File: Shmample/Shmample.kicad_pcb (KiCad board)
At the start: 2 copper layers, 127 x 127 mm, 148 parts, among them J1 Conn_01x04_Socket, J2 PowerOut, Q1 BC547, Q10 BC547, Q2 BC557, Q3 BC547, Q4 BC547, Q5 BC557, Q6 BC557, Q7 BC547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

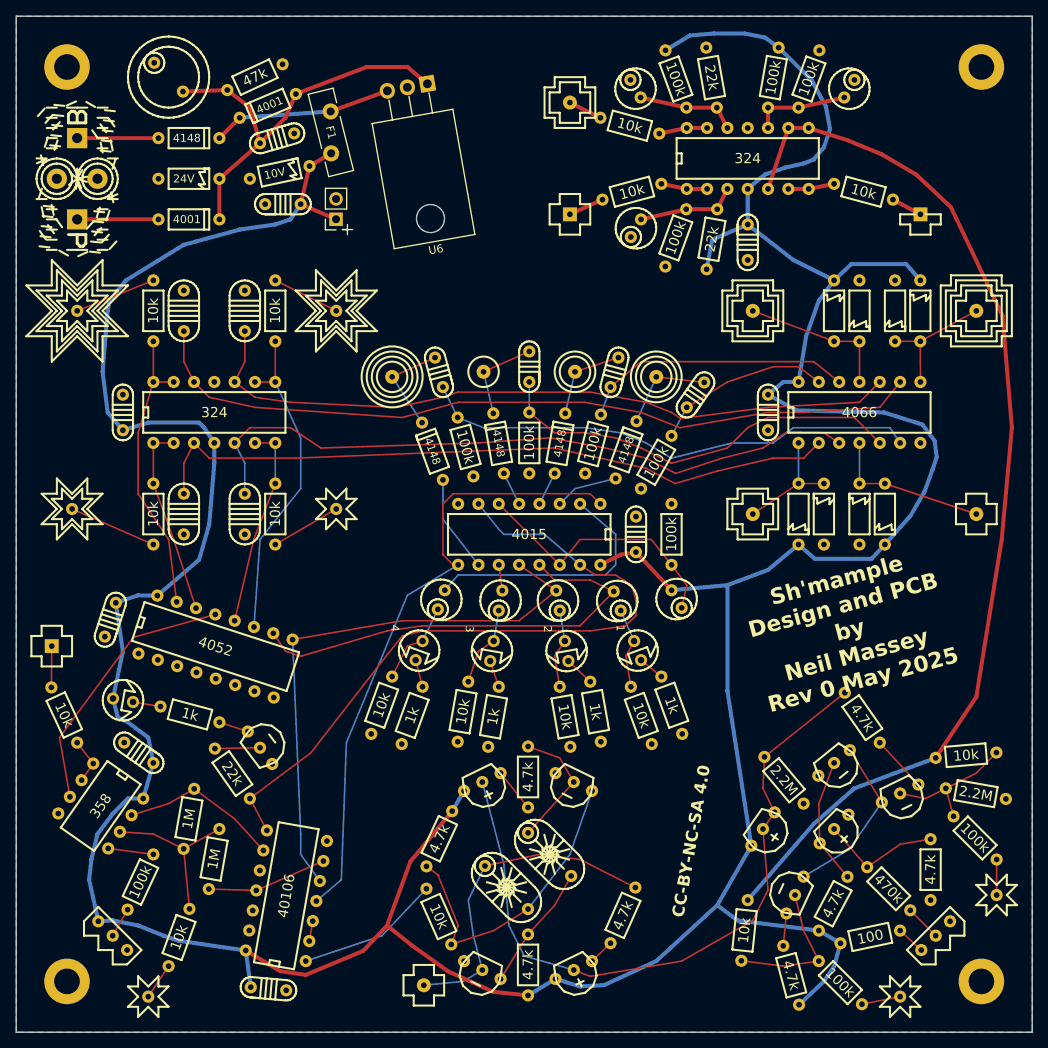
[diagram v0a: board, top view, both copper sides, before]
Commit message: Added attenuators
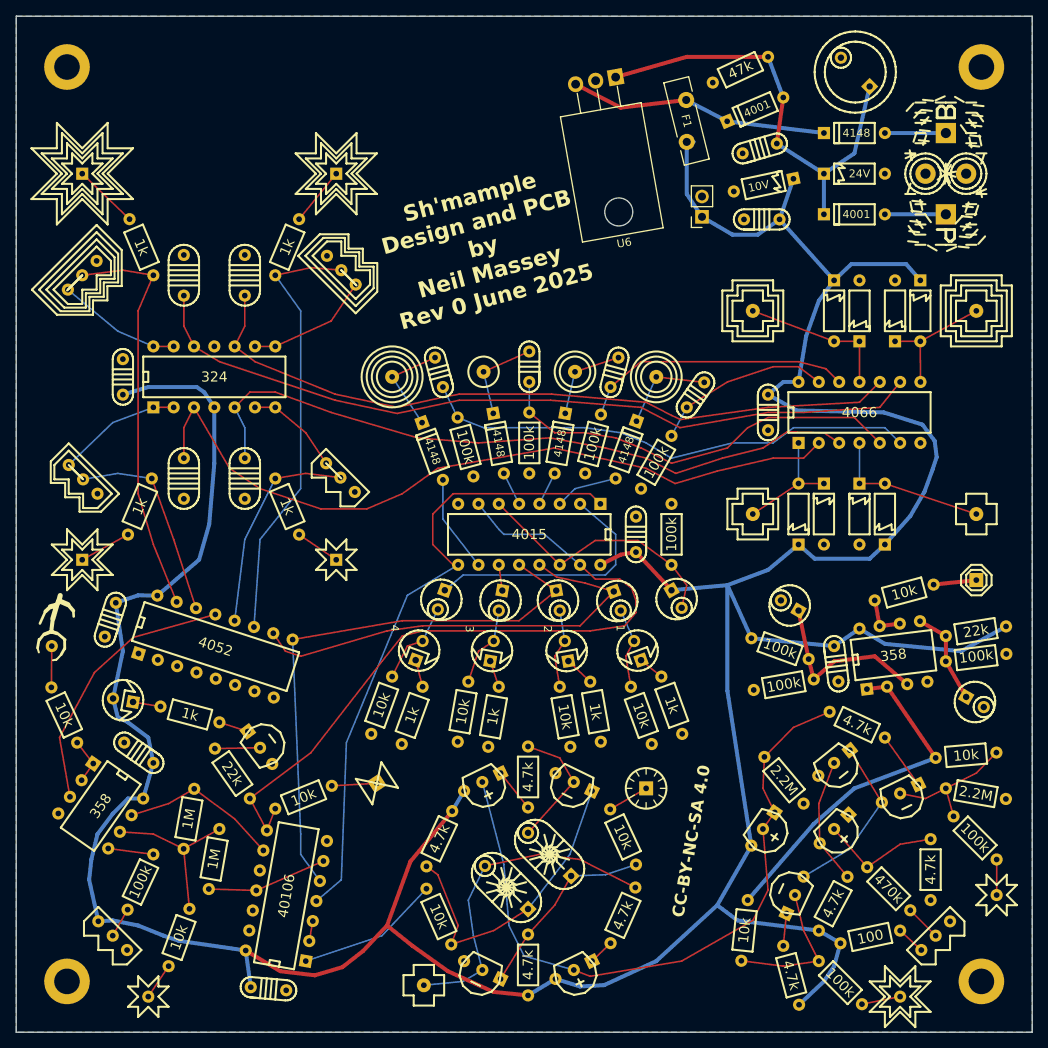
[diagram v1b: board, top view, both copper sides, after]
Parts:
- removed C18: 10uF, diy-nabra:cel1
- removed R40: 22k, diy-nabra:r3
- removed R51: 10k, diy-nabra:r3
- added RV3: 4_W, diy-nabra:wnob4, F.Cu at (19.2, 46.9)
- added RV4: 3_W, diy-nabra:wnob3, F.Cu at (55.1, 46.2)
- added RV5: 2_W, diy-nabra:wnob2, F.Cu at (19.3, 68.8)
- added RV6: 1_W, diy-nabra:wnob1, F.Cu at (51.4, 68.6)
- R33, R34, R35, R36: value 10k -> 1k
- R39: value 100k -> 10k
- TP1: footprint diy-nabra:wtrin -> diy-nabra:wtrin2
- TP12: value Lo -> Cmp-Out; footprint diy-nabra:wsqu2in -> diy-nabra:wcmp_out
- TP13: footprint diy-nabra:wsqout -> diy-nabra:wvout
- TP19: footprint diy-nabra:wsqout -> diy-nabra:wpod
- TP20: value MIDO -> Clk-Out; footprint diy-nabra:wsqout -> diy-nabra:wclk_out
- U1: value 324 -> 358; footprint diy-nabra:dip14 -> diy-nabra:dip8
- moved J1 108.6 mm to (128.9, 37.5)
- moved R49 97.1 mm to (45.1, 111.8), turned to 22 degrees
- moved R39 95.1 mm to (86.9, 111.8), turned to -65 degrees
- moved TP12 88.4 mm to (57.8, 108.6), turned to 33 degrees
- moved C19 85.8 mm to (115.8, 17.9)
- moved TP20 79.5 mm to (91.4, 109.2)
- moved D8 75.6 mm to (113.7, 32.4), turned to 0 degrees
- moved D6 75.6 mm to (113.7, 37.5), turned to 0 degrees
- moved D9 75.6 mm to (113.7, 27.3), turned to 0 degrees
- moved R3 73.9 mm to (104.6, 90.5), turned to -20 degrees
- moved C17 73.5 mm to (133.6, 99.1), turned to 150 degrees
- moved R4 71.5 mm to (112.4, 95.6), turned to -170 degrees
- moved TP13 68.3 mm to (132.7, 83.2)
- moved U1 66.2 mm to (118.1, 89.3), turned to 7 degrees
- moved C1 65.7 mm to (108.3, 85.7), turned to -30 degrees
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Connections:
- C1 pad 1: Net-(U1C-+) -> Net-(U1A-+)
- C17 pad 1: Net-(U1A-+) -> Net-(U1B-+)
- R3 pad 1: Net-(U1C-+) -> Net-(U1A-+)
- R33 pad 1: Net-(U5B--) -> Net-(U7-X0)
- R34 pad 1: Net-(U5A--) -> Net-(U7-X1)
- R35 pad 1: Net-(U5C--) -> Net-(U7-X3)
- R36 pad 1: Net-(U5D--) -> Net-(U7-X2)
- R37 pad 1: Net-(U1A-+) -> Net-(U1B-+)
- R38 pad 2: Net-(U1A-+) -> Net-(U1B-+)
- R39 pad 1: Net-(U1D-+) -> Net-(Q7-C)
- R39 pad 2: +9V -> Net-(R39-Pad2)
- R4 pad 2: Net-(U1C-+) -> Net-(U1A-+)
- R49 pad 2: Lo -> Data
- TP20 pad 1: Net-(R51-Pad1) -> Net-(R39-Pad2)
- U1 pad 1: Hi -> MIDO
- U1 pad 2: Hi -> MIDO
- U1 pad 4: +9V -> GND
- U1 pad 5: MIDO -> Net-(U1B-+)
- U1 pad 6: MIDO2 -> Hi
- U1 pad 7: MIDO2 -> Hi
- U1 pad 8: MIDO -> +9V
- U7 pad 11: Net-(U5C--) -> Net-(U7-X3)
- U7 pad 12: Net-(U5B--) -> Net-(U7-X0)
- U7 pad 14: Net-(U5A--) -> Net-(U7-X1)
- U7 pad 15: Net-(U5D--) -> Net-(U7-X2)
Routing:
- net MIDO: track 133.6 -> 43.5 mm
- net Net-(U7-X3): track 0.00 -> 55.2 mm
- net Net-(U7-X2): track 0.00 -> 51.0 mm
- net +9V: track 498.4 -> 456.8 mm
- net Net-(U7-X0): track 0.00 -> 27.0 mm
- net Net-(U7-X1): track 0.00 -> 25.8 mm
- net Net-(U5C--): track 40.7 -> 15.7 mm
- net Net-(U5D--): track 36.6 -> 15.5 mm
- net Net-(U5B--): track 25.5 -> 12.1 mm
- net Net-(U1D-+): track 12.5 -> 0.00 mm
- net Net-(U1C-+): track 12.2 -> 0.00 mm
- net Net-(U1B-+): track 0.00 -> 12.0 mm
- net Net-(U1A-+): track 12.5 -> 22.7 mm
- net Net-(D7-K): track 22.5 -> 32.5 mm
- net Net-(U5A--): track 24.1 -> 15.6 mm
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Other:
- board text added: "Sh'mample Design and PCB by Neil Massey Rev 0 June 2025"
- board text removed: "Sh'mample Design and PCB by Neil Massey Rev 0 May 2025"

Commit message: Revision
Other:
- board text added: "SAnnddmedaedSalAHHHHdSedaaAHddmpnHlmnldpeeopd dSAoamlnSldldpHandeodddSleAAAlSmAdSAolmlHdpAo dpnndaelplHooaaAHllSampleAndHoldmpHmllnHmnopn dldaAdldenoalndddelleeolSSaAHdddmeoSpAHHlappH oplldlmedSlnooSmdHomlAlmddodlddlAoalAAHHlldda Adddlldddaeoanldmdl An SleennSeHaaedddSAl Smnddoldllnopda mndlldloopleeAAd AnHSAdpdodSAHaandS eHmAHSaaenHSmpH mAdHSpHoSpno mnooSedodeA"

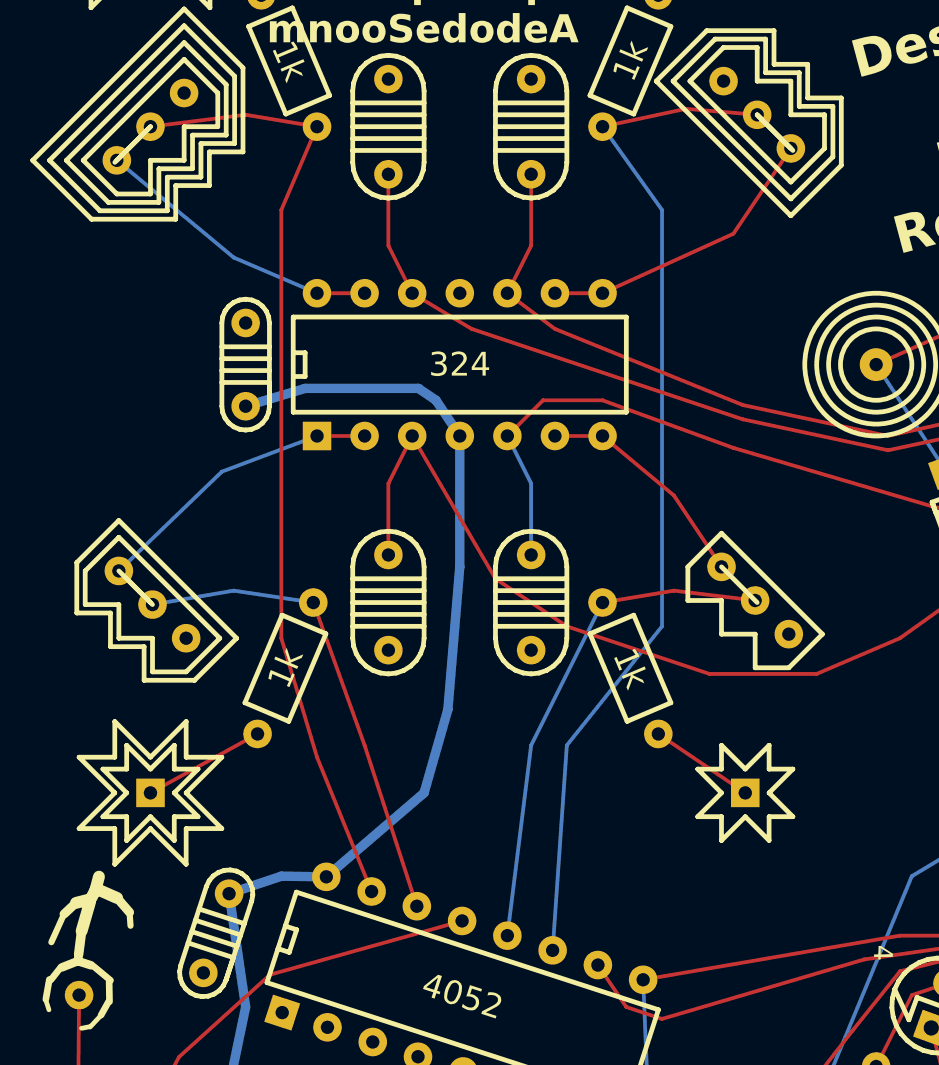
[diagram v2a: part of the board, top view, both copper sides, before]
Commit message: Rotated a pot.  That is all
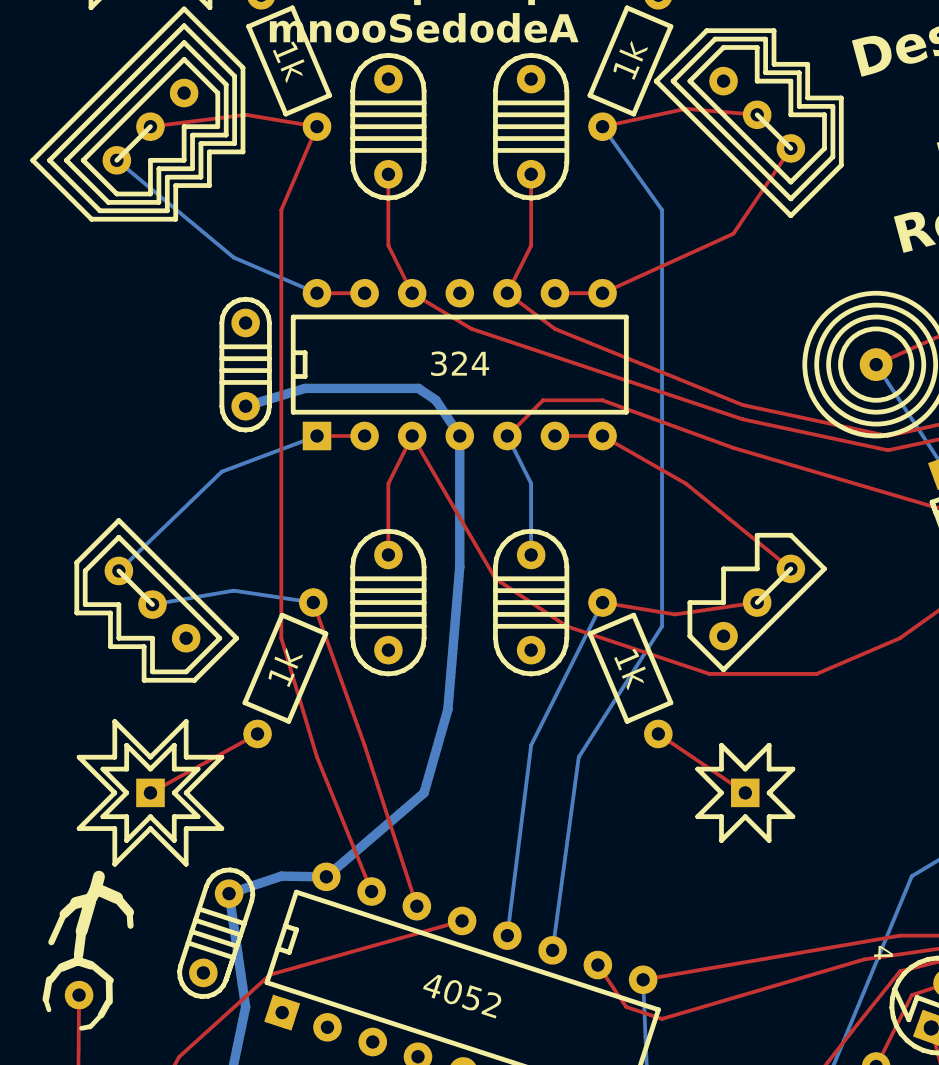
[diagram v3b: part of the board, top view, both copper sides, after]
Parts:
- moved RV6 3.70 mm to (55.1, 68.7), turned to -135 degrees
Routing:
- net Net-(U5B--): track 12.1 -> 14.9 mm
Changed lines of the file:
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@@
 	(footprint "diy-nabra:wnob1"
 		(layer "F.Cu")
-		(at 51.435 68.58 -45)
+		(at 55.136051 68.688949 -135)
 		(descr "wnob from Ciat-Lonbarde Osmond PCB library")
 		(tags "wnob from Ciat-Lonbarde Osmond PCB library")
 		(property "Reference" "RV6"
-			(at 2.54 3.81 315)
+			(at 2.54 3.81 45)
 			(layer "F.Fab")
 			(effects
@@
 		)
 		(property "Value" "1_W"
-			(at 2.54 -2.54 315)
+			(at 2.54 -2.54 45)
 			(layer "F.SilkS")
 			(hide yes)
@@
 		)
 		(property "Datasheet" ""
-			(at 0 0 315)
+			(at 0 0 45)
 			(layer "F.Fab")
 			(hide yes)
@@
 		)
 		(property "Description" ""
-			(at 0 0 315)
+			(at 0 0 45)
 			(layer "F.Fab")
 			(hide yes)
@@
 		(attr through_hole)
 		(fp_line
-			(start -1.27 1.27)
-			(end 0 2.54)
+			(start 5.08 2.54)
+			(end 6.35 1.270001)
 			(stroke
 				(width 0.254)
@@
 		)
 		(fp_line
-			(start 0 2.54)
-			(end 1.27 1.27)
+			(start 6.35 1.270001)
+			(end 6.35 -1.270001)
 			(stroke
 				(width 0.254)
@@
 		)
 		(fp_line
-			(start -1.27 -1.27)
-			(end -1.27 1.27)
+			(start 2.54 2.54)
+			(end 3.81 1.27)
 			(stroke
 				(width 0.254)
@@
 		)
 		(fp_line
-			(start 1.27 1.27)
-			(end 2.54 2.54)
+			(start 3.81 1.27)
+			(end 5.08 2.54)
 			(stroke
 				(width 0.254)
@@
 		)
 		(fp_line
-			(start 2.54 2.54)
-			(end 3.81 1.27)
+			(start 6.35 -1.270001)
+			(end -1.27 -1.27)
 			(stroke
 				(width 0.254)
@@
 		)
 		(fp_line
-			(start 2.54 0)
-			(end 0 0)
+			(start 0 2.54)
+			(end 1.27 1.27)
 			(stroke
-				(width 0.12)
+				(width 0.254)
 				(type default)
 			)
@@
 		)
 		(fp_line
-			(start 3.81 1.27)
-			(end 5.08 2.54)
+			(start 1.27 1.27)
+			(end 2.54 2.54)
 			(stroke
 				(width 0.254)
@@
 		)
 		(fp_line
-			(start 5.08 2.54)
-			(end 6.35 1.270001)
+			(start 2.54 0)
+			(end 0 0)
 			(stroke
 				(width 0.254)
-				(type default)
+				(type solid)
 			)
 			(layer "F.SilkS")
 		)
 		(fp_line
-			(start 6.35 1.270001)
-			(end 6.35 -1.270001)
+			(start -1.27 1.27)
+			(end 0 2.54)
 			(stroke
 				(width 0.254)
@@
 		)
 		(fp_line
-			(start 6.35 -1.270001)
-			(end -1.27 -1.27)
+			(start -1.27 -1.27)
+			(end -1.27 1.27)
 			(stroke
 				(width 0.254)
@@
 		)
 		(pad "1" thru_hole circle
-			(at 5.079999 0 315)
+			(at 5.079999 0 225)
 			(size 1.524 1.524)
 			(drill 0.7112)
@@
 		)
 		(pad "2" thru_hole circle
-			(at 2.54 0 315)
+			(at 2.54 0 225)
 			(size 1.524 1.524)
 			(drill 0.7112)
@@
 		)
 		(pad "3" thru_hole circle
-			(at 0 0 315)
+			(at 0 0 225)
 			(size 1.524 1.524)
 			(drill 0.7112)
@@
 		)
 		(fp_line
-			(start 0.49786 -1.648802)
+			(start 0.49786 -1.648803)
 			(end 1.51426 -1.068)
 			(stroke
@@
 	)
 	(gr_line
-		(start 51.435 68.58)
-		(end 53.34 70.485)
-		(stroke
-			(width 0.254)
-			(type solid)
-		)
-		(layer "F.SilkS")
-	)
-	(gr_line
-		(start 20.955 70.485)
-		(end 19.685 69.215)
-		(stroke
-			(width 0.254)
-			(type solid)
-		)
-		(layer "F.SilkS")
-	)
-	(gr_line
-		(start 19.05 46.99)
-		(end 20.955 45.085)
-		(stroke
-			(width 0.254)
-			(type solid)
-		)
-		(layer "F.SilkS")
-	)
-	(gr_line
-		(start 53.34 44.45)
-		(end 55.245 46.355)
-		(stroke
-			(width 0.254)
-			(type solid)
-		)
-		(layer "F.SilkS")
-	)
-	(gr_line
 		(start 93.384515 35.239287)
 		(end 93.384515 35.874287)
@@
 	)
 	(segment
-		(start 48.895 64.77)
+		(start 49.53 64.135)
 		(end 45.085 61.595)
 		(width 0.2)
@@
 	)
 	(segment
-		(start 51.435 68.58)
-		(end 48.895 64.77)
+		(start 55.136051 68.688949)
+		(end 49.53 64.135)
 		(width 0.2)
 		(layer "F.Cu")
@@
 	)
 	(segment
-		(start 48.895 69.85)
-		(end 53.231051 70.376051)
+		(start 45.085 70.485)
+		(end 48.95007 71.12)
 		(width 0.2)
 		(layer "F.Cu")
@@
 	)
 	(segment
-		(start 45.085 70.485)
-		(end 48.895 69.85)
+		(start 48.95007 71.12)
+		(end 53.34 70.485)
+		(width 0.2)
+		(layer "F.Cu")
+		(net 86)
+	)
+	(segment
+		(start 53.34 70.485)
+		(end 53.231051 70.376051)
 		(width 0.2)
 		(layer "F.Cu")
@@
 	)
 	(segment
-		(start 42.420684 89.049903)
-		(end 43.18 78.105)
+		(start 43.815 78.74)
+		(end 48.26 71.755)
 		(width 0.2)
 		(layer "B.Cu")
@@
 	)
 	(segment
-		(start 43.18 78.105)
-		(end 48.26 71.755)
+		(start 48.26 71.755)
+		(end 48.26 49.53)
 		(width 0.2)
 		(layer "B.Cu")
@@
 	)
 	(segment
-		(start 48.26 49.53)
-		(end 45.085 45.085)
+		(start 42.420684 89.049903)
+		(end 43.815 78.74)
 		(width 0.2)
 		(layer "B.Cu")
@@
 	)
 	(segment
-		(start 48.26 71.755)
-		(end 48.26 49.53)
+		(start 48.26 49.53)
+		(end 45.085 45.085)
 		(width 0.2)
 		(layer "B.Cu")
